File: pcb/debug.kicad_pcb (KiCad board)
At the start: 4 copper layers, 50 x 100 mm, 70 parts, among them J1 09032967825, J2 USB_C_Receptacle_USB2.0, Q1 Q_PNP_BCE, SW1 SW_DIP_x02, SW2 Reset, U1 STLQ020PU33R, U2 FT4222HQ, U3 STM32F103V8Tx, U4 INA381AxDSG, U5 SN74ALVC00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

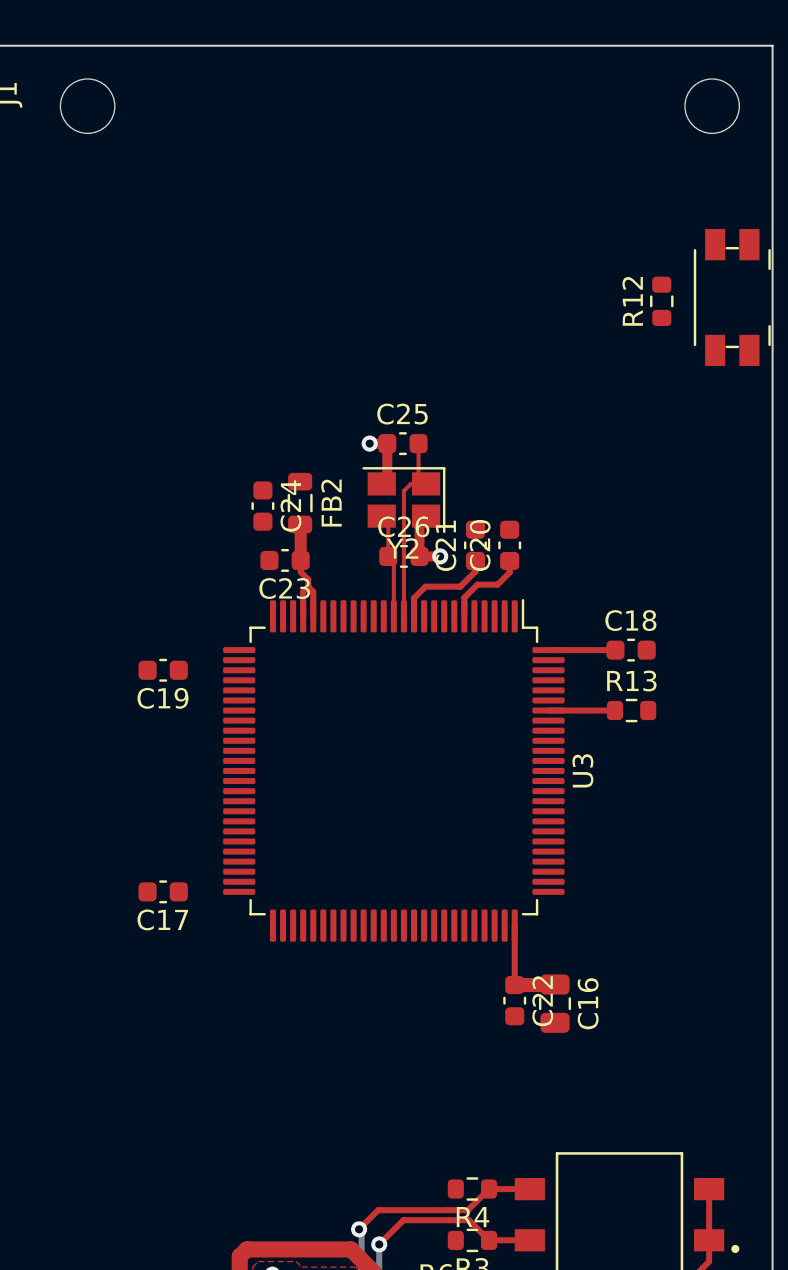
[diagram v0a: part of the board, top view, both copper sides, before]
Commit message: add SWD
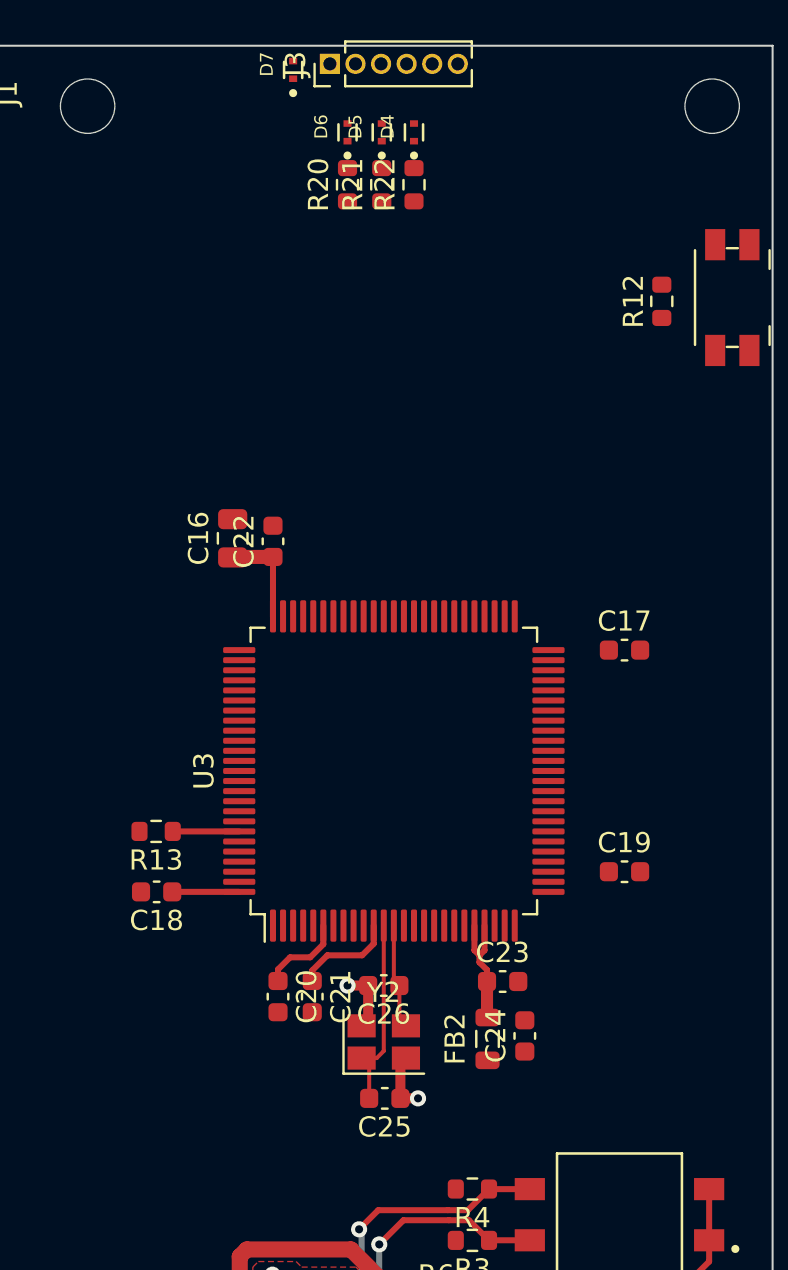
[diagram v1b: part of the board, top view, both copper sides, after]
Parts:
- added D4: D_TVS, SOD-923-2:TVS_ESD9D5.0ST5G, F.Cu at (111.2, 53.3)
- added D5: D_TVS, SOD-923-2:TVS_ESD9D5.0ST5G, F.Cu at (109.6, 53.3)
- added D6: D_TVS, SOD-923-2:TVS_ESD9D5.0ST5G, F.Cu at (107.9, 53.3)
- added D7: D_TVS, SOD-923-2:TVS_ESD9D5.0ST5G, F.Cu at (105.2, 50.2)
- added J3: Conn_01x06_Female, Connector_PinHeader_1.27mm:PinHeader_1x06_P1.27mm_Vertical, F.Cu at (107.0, 49.9)
- added R20: 220, Resistor_SMD:R_0603_1608Metric, F.Cu at (107.9, 55.9)
- added R21: 220, Resistor_SMD:R_0603_1608Metric, F.Cu at (109.6, 55.9)
- added R22: 220, Resistor_SMD:R_0603_1608Metric, F.Cu at (111.2, 55.9)
- moved C25 32.5 mm to (109.8, 101.2), turned to 180 degrees
- moved C24 29.3 mm to (116.7, 98.2), turned to 90 degrees
- moved FB2 28.2 mm to (114.8, 98.3), turned to -90 degrees
- moved C16 28.1 mm to (102.2, 73.5), turned to 90 degrees
- moved Y2 26.9 mm to (109.7, 98.5), turned to 0 degrees
- moved C18 26.4 mm to (98.4, 91.0), turned to 180 degrees
- moved C17 25.9 mm to (121.7, 79.0), turned to 0 degrees
- moved C22 25.8 mm to (104.2, 73.6), turned to 90 degrees
- moved C20 25.2 mm to (104.5, 96.2), turned to -90 degrees
- moved C19 25.0 mm to (121.7, 90.0), turned to 0 degrees
- moved R13 24.4 mm to (98.4, 88.0), turned to 180 degrees
- moved C21 23.8 mm to (106.2, 96.2), turned to -90 degrees
- moved C23 23.5 mm to (115.6, 95.5), turned to 0 degrees
- moved C26 21.3 mm to (109.7, 95.7), turned to 180 degrees
- turned U3 to 90 degrees
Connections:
- U3 pad 1: CONN_44 -> unconnected-(U3-Pad1)
- U3 pad 15: CONN_28 -> unconnected-(U3-Pad15)
- U3 pad 16: CONN_29 -> unconnected-(U3-Pad16)
- U3 pad 17: CONN_30 -> unconnected-(U3-Pad17)
- U3 pad 18: CONN_31 -> unconnected-(U3-Pad18)
- U3 pad 2: CONN_45 -> unconnected-(U3-Pad2)
- U3 pad 23: CONN_0 -> unconnected-(U3-Pad23)
- U3 pad 24: CONN_1 -> unconnected-(U3-Pad24)
- U3 pad 25: CONN_2 -> unconnected-(U3-Pad25)
- U3 pad 26: CONN_3 -> unconnected-(U3-Pad26)
- U3 pad 3: CONN_46 -> unconnected-(U3-Pad3)
- U3 pad 33: CONN_32 -> MODULE_ENABLE
- U3 pad 34: CONN_33 -> MODULE_RESET
- U3 pad 35: CONN_12 -> CURRENT_SENSE
- U3 pad 36: CONN_13 -> unconnected-(U3-Pad36)
- U3 pad 37: CONN_14 -> unconnected-(U3-Pad37)
- U3 pad 38: CONN_49 -> unconnected-(U3-Pad38)
- U3 pad 39: CONN_50 -> unconnected-(U3-Pad39)
- U3 pad 4: CONN_47 -> unconnected-(U3-Pad4)
- U3 pad 40: CONN_51 -> unconnected-(U3-Pad40)
- U3 pad 41: CONN_52 -> unconnected-(U3-Pad41)
- U3 pad 47: CONN_22 -> unconnected-(U3-Pad47)
- U3 pad 48: CONN_23 -> unconnected-(U3-Pad48)
- U3 pad 5: CONN_48 -> unconnected-(U3-Pad5)
- U3 pad 51: CONN_24 -> unconnected-(U3-Pad51)
- U3 pad 52: CONN_25 -> unconnected-(U3-Pad52)
- U3 pad 53: CONN_26 -> unconnected-(U3-Pad53)
- U3 pad 54: CONN_27 -> unconnected-(U3-Pad54)
- U3 pad 63: CONN_34 -> unconnected-(U3-Pad63)
- U3 pad 64: CONN_35 -> unconnected-(U3-Pad64)
- U3 pad 65: CONN_36 -> unconnected-(U3-Pad65)
- U3 pad 66: CONN_37 -> unconnected-(U3-Pad66)
- U3 pad 67: CONN_4 -> unconnected-(U3-Pad67)
- U3 pad 68: CONN_5 -> unconnected-(U3-Pad68)
- U3 pad 69: CONN_6 -> unconnected-(U3-Pad69)
- U3 pad 7: CONN_41 -> unconnected-(U3-Pad7)
- U3 pad 70: CONN_7 -> unconnected-(U3-Pad70)
- U3 pad 71: CONN_8 -> unconnected-(U3-Pad71)
- U3 pad 72: CONN_9 -> /MCU/MCU_SWDIO
- U3 pad 76: CONN_10 -> /MCU/MCU_SWCLK
- U3 pad 77: CONN_11 -> unconnected-(U3-Pad77)
- U3 pad 78: CONN_38 -> unconnected-(U3-Pad78)
- U3 pad 79: CONN_39 -> unconnected-(U3-Pad79)
- U3 pad 8: CONN_42 -> unconnected-(U3-Pad8)
- U3 pad 80: CONN_40 -> unconnected-(U3-Pad80)
- U3 pad 81: MODULE_ENABLE -> unconnected-(U3-Pad81)
- U3 pad 82: MODULE_RESET -> unconnected-(U3-Pad82)
- U3 pad 89: CONN_15 -> /MCU/MCU_SWTRACE
- U3 pad 9: CONN_43 -> unconnected-(U3-Pad9)
- U3 pad 90: CONN_16 -> unconnected-(U3-Pad90)
- U3 pad 91: CONN_17 -> unconnected-(U3-Pad91)
- U3 pad 92: CONN_18 -> unconnected-(U3-Pad92)
- U3 pad 93: CONN_19 -> unconnected-(U3-Pad93)
- U3 pad 95: CONN_20 -> unconnected-(U3-Pad95)
- U3 pad 96: CONN_21 -> unconnected-(U3-Pad96)

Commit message: add bus traces
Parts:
- moved R13 9.21 mm to (102.6, 96.2), turned to -90 degrees
- moved C16 3.12 mm to (100.4, 76.0)
- moved C18 2.81 mm to (100.5, 92.9)
- moved C22 2.78 mm to (102.5, 75.8)
- moved C17 0.45 mm to (121.2, 79.0)
- moved C19 0.35 mm to (121.3, 90.0)
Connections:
- U3 pad 65: unconnected-(U3-Pad65) -> CONN_52
- U3 pad 66: unconnected-(U3-Pad66) -> CONN_51
- U3 pad 67: unconnected-(U3-Pad67) -> CONN_50
- U3 pad 68: unconnected-(U3-Pad68) -> CONN_49
- U3 pad 69: unconnected-(U3-Pad69) -> CONN_48
- U3 pad 70: unconnected-(U3-Pad70) -> CONN_47
- U3 pad 71: unconnected-(U3-Pad71) -> CONN_46
- U3 pad 77: unconnected-(U3-Pad77) -> CONN_45
- U3 pad 78: unconnected-(U3-Pad78) -> CONN_44
- U3 pad 79: unconnected-(U3-Pad79) -> CONN_43
- U3 pad 80: unconnected-(U3-Pad80) -> CONN_42
- U3 pad 81: unconnected-(U3-Pad81) -> CONN_41
- U3 pad 82: unconnected-(U3-Pad82) -> CONN_40
- U3 pad 83: unconnected-(U3-Pad83) -> CONN_39
- U3 pad 84: unconnected-(U3-Pad84) -> CONN_38
- U3 pad 85: unconnected-(U3-Pad85) -> CONN_37
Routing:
- net CONN_51: track 0.00 -> 29.3 mm
- net CONN_48: track 0.00 -> 26.7 mm
- net CONN_49: track 0.00 -> 25.1 mm
- net CONN_52: track 0.00 -> 24.5 mm
- net CONN_47: track 0.00 -> 23.8 mm
- net CONN_50: track 0.00 -> 22.8 mm
- net unconnected-(U3-Pad93): track 0.00 -> 22.4 mm
- net unconnected-(U3-Pad90): track 0.00 -> 21.8 mm
- net unconnected-(U3-Pad86): track 0.00 -> 20.7 mm
- net unconnected-(U3-Pad95): track 0.00 -> 20.3 mm
- net CONN_46: track 0.00 -> 20.1 mm
- net CONN_39: track 0.00 -> 20.0 mm
- net unconnected-(U3-Pad92): track 0.00 -> 19.8 mm
- net CONN_45: track 0.00 -> 18.9 mm
- net unconnected-(U3-Pad87): track 0.00 -> 18.8 mm
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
